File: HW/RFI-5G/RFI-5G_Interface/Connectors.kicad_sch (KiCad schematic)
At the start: 5 parts, among them J1 Conn_01x10_Female, J2 Conn_01x10_Female, J3 Conn_01x10_Female, J4 Conn_01x10_Female, J5 Conn_01x04_Female

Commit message: RF top and Bottom boards
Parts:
- removed J1, J2, J3, J4: Conn_01x10_Female, Connector_PinHeader_2.54mm:PinHeader_1x10_P2.54mm_Vertical, symbol Connector:Conn_01x10_Female
- removed J5: Conn_01x04_Female, Connector_PinHeader_2.54mm:PinHeader_1x04_P2.54mm_Vertical, symbol Connector:Conn_01x04_Female
- added J1, J4: Conn_01x03, Connector_PinHeader_2.54mm:PinHeader_1x03_P2.54mm_Vertical, symbol Connector_Generic:Conn_01x03
- added J2: Conn_01x02, Connector_PinHeader_2.54mm:PinHeader_1x02_P2.54mm_Vertical, symbol Connector_Generic:Conn_01x02
- added J3: Conn_01x10, Connector_PinHeader_2.54mm:PinHeader_1x10_P2.54mm_Vertical, symbol Connector_Generic:Conn_01x10
- added J5: Conn_01x06_Female, Connector_PinHeader_1.00mm:PinHeader_1x06_P1.00mm_Vertical, symbol Connector:Conn_01x06_Female
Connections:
- net ADC_PL2: now also J4.2 (Pin_2)
- net DAC_PL2: now also J4.3 (Pin_3)
- net GND: now also J1.3 (Pin_3), J2.1 (Pin_1), J3.10 (Pin_10), J3.3 (Pin_3), J3.4 (Pin_4), J4.1 (Pin_1)
- net SCL: now also J1.2 (Pin_2)
- net SDA: now also J1.1 (Pin_1)
- net VCC: now also J2.2 (Pin_2)
- new net 2V5: J5.2 (Pin_2)
- new net 2V7: J5.4 (Pin_4)
- new net 2V75: J3.1 (Pin_1), J5.6 (Pin_6)
- new net 3V: J3.8 (Pin_8)
- new net LDO_extra1: J5.3 (Pin_3)
- new net LDO_extra2: J5.5 (Pin_5)
- new net LEE1_Vcc: J3.6 (Pin_6)
- new net LEE2_Vcc: J3.7 (Pin_7)
- new net P/L power: J3.5 (Pin_5)
- new net RSSI: J3.9 (Pin_9)
- new net Vtune1: J5.1 (Pin_1)
- new net Vtune2: J3.2 (Pin_2)
- no-connect marks 11 -> 0
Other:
- note added: "Vcc will need to be changed to PoL whena pin for the point of load is available. Also, in the PCB, the Vcc zone will have to be changed to PoL."

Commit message: PL boards
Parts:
- removed J5: Conn_01x06_Female, Connector_PinHeader_1.00mm:PinHeader_1x06_P1.00mm_Vertical, symbol Connector:Conn_01x06_Female
- added J5: Conn_01x10_Female, Connector_PinHeader_1.00mm:PinHeader_1x10_P1.00mm_Vertical, symbol Connector:Conn_01x10_Female
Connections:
- net 3V: now also J5.8 (Pin_8)
- net GND: now also J5.7 (Pin_7)
- net SCL: now also J5.10 (Pin_10)
- net SDA: now also J5.9 (Pin_9)
- new net VTune1: J5.2 (Pin_2)
- new net Vcc_IF1Amp: J5.1 (Pin_1)
- new net Vcc_LNA1: J5.6 (Pin_6)
- new net Vcc_LNA2: J5.5 (Pin_5)
- new net Vcc_LO1Amp: J5.4 (Pin_4)
- new net Vcc_VCO: J5.3 (Pin_3)
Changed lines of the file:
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@@
+    (stroke (width 0) (type default) (color 0 0 0 0))
+  )
+  (wire (pts (xy 184.15 76.2) (xy 191.77 76.2))
     (stroke (width 0) (type default) (color 0 0 0 0))
   )
@@
     )
   )
-  (global_label "LDO_extra1" (shape input) (at 194.31 69.85 180) (fields_autoplaced)
-    (effects (font (size 1.27 1.27)) (justify right))
-    (property "Intersheet References" "${INTERSHEET_REFS}" (id 0) (at 181.3136 69.7706 0)
-      (effects (font (size 1.27 1.27)) (justify right) hide)
-    )
-  )
   (global_label "RSSI" (shape input) (at 151.13 93.98 90) (fields_autoplaced)
     (effects (font (size 1.27 1.27)) (justify left))
@@
     )
   )
-  (global_label "Vtune1" (shape input) (at 194.31 64.77 180) (fields_autoplaced)
-    (effects (font (size 1.27 1.27)) (justify right))
-    (property "Intersheet References" "${INTERSHEET_REFS}" (id 0) (at 185.4864 64.6906 0)
-      (effects (font (size 1.27 1.27)) (justify right) hide)
-    )
-  )
   (global_label "SCL" (shape bidirectional) (at 133.35 57.15 270) (fields_autoplaced)
     (effects (font (size 1.27 1.27)) (justify right))
@@
     )
   )
+  (global_label "SDA" (shape bidirectional) (at 191.77 81.28 180) (fields_autoplaced)
+    (effects (font (size 1.27 1.27)) (justify right))
+    (property "Intersheet References" "${INTERSHEET_REFS}" (id 0) (at 185.7888 81.2006 0)
+      (effects (font (size 1.27 1.27)) (justify right) hide)
+    )
+  )
   (global_label "LEE2_Vcc" (shape input) (at 146.05 93.98 90) (fields_autoplaced)
     (effects (font (size 1.27 1.27)) (justify left))
@@
     )
   )
-  (global_label "2V7" (shape input) (at 194.31 72.39 180) (fields_autoplaced)
-    (effects (font (size 1.27 1.27)) (justify right))
-    (property "Intersheet References" "${INTERSHEET_REFS}" (id 0) (at 188.3893 72.3106 0)
+  (global_label "Vcc_LNA1" (shape input) (at 191.77 73.66 180) (fields_autoplaced)
+    (effects (font (size 1.27 1.27)) (justify right))
+    (property "Intersheet References" "${INTERSHEET_REFS}" (id 0) (at 180.4669 73.5806 0)
       (effects (font (size 1.27 1.27)) (justify right) hide)
     )
@@
     )
   )
-  (global_label "2V75" (shape input) (at 194.31 77.47 180) (fields_autoplaced)
-    (effects (font (size 1.27 1.27)) (justify right))
-    (property "Intersheet References" "${INTERSHEET_REFS}" (id 0) (at 187.1798 77.3906 0)
+  (global_label "3V" (shape input) (at 191.77 78.74 180) (fields_autoplaced)
+    (effects (font (size 1.27 1.27)) (justify right))
+    (property "Intersheet References" "${INTERSHEET_REFS}" (id 0) (at 187.0588 78.6606 0)
       (effects (font (size 1.27 1.27)) (justify right) hide)
     )
@@
     )
   )
-  (global_label "2V5" (shape input) (at 194.31 67.31 180) (fields_autoplaced)
-    (effects (font (size 1.27 1.27)) (justify right))
-    (property "Intersheet References" "${INTERSHEET_REFS}" (id 0) (at 188.3893 67.2306 0)
+  (global_label "SCL" (shape bidirectional) (at 191.77 83.82 180) (fields_autoplaced)
+    (effects (font (size 1.27 1.27)) (justify right))
+    (property "Intersheet References" "${INTERSHEET_REFS}" (id 0) (at 185.8493 83.7406 0)
+      (effects (font (size 1.27 1.27)) (justify right) hide)
+    )
+  )
+  (global_label "Vcc_LNA2" (shape input) (at 191.77 71.12 180) (fields_autoplaced)
+    (effects (font (size 1.27 1.27)) (justify right))
+    (property "Intersheet References" "${INTERSHEET_REFS}" (id 0) (at 180.4669 71.0406 0)
       (effects (font (size 1.27 1.27)) (justify right) hide)
     )
@@
     )
   )
-  (global_label "LDO_extra2" (shape input) (at 194.31 74.93 180) (fields_autoplaced)
-    (effects (font (size 1.27 1.27)) (justify right))
-    (property "Intersheet References" "${INTERSHEET_REFS}" (id 0) (at 181.3136 74.8506 0)
+  (global_label "Vcc_IF1Amp" (shape input) (at 191.77 60.96 180) (fields_autoplaced)
+    (effects (font (size 1.27 1.27)) (justify right))
+    (property "Intersheet References" "${INTERSHEET_REFS}" (id 0) (at 178.2898 60.8806 0)
+      (effects (font (size 1.27 1.27)) (justify right) hide)
+    )
+  )
+  (global_label "Vcc_LO1Amp" (shape input) (at 191.77 68.58 180) (fields_autoplaced)
+    (effects (font (size 1.27 1.27)) (justify right))
+    (property "Intersheet References" "${INTERSHEET_REFS}" (id 0) (at 177.6245 68.5006 0)
+      (effects (font (size 1.27 1.27)) (justify right) hide)
+    )
+  )
+  (global_label "VTune1" (shape input) (at 191.77 63.5 180) (fields_autoplaced)
+    (effects (font (size 1.27 1.27)) (justify right))
+    (property "Intersheet References" "${INTERSHEET_REFS}" (id 0) (at 182.7045 63.4206 0)
+      (effects (font (size 1.27 1.27)) (justify right) hide)
+    )
+  )
+  (global_label "Vcc_VCO" (shape input) (at 191.77 66.04 180) (fields_autoplaced)
+    (effects (font (size 1.27 1.27)) (justify right))
+    (property "Intersheet References" "${INTERSHEET_REFS}" (id 0) (at 181.4345 65.9606 0)
       (effects (font (size 1.27 1.27)) (justify right) hide)
     )
@@
     (pin "3")
   )
-  (symbol (lib_id "Connector:Conn_01x06_Female") (at 199.39 69.85 0) (unit 1)
+  (symbol (lib_id "power:GND") (at 184.15 76.2 270) (unit 1)
+    (in_bom yes) (on_board yes)
+    (property "Reference" "#PWR?" (id 0) (at 177.8 76.2 0)
+      (effects (font (size 1.27 1.27)) hide)
+    )
+    (property "Value" "GND" (id 1) (at 179.07 74.93 0)
+      (effects (font (size 1.27 1.27)) (justify left))
+    )
+    (property "Footprint" "" (id 2) (at 184.15 76.2 0)
+      (effects (font (size 1.27 1.27)) hide)
+    )
+    (property "Datasheet" "" (id 3) (at 184.15 76.2 0)
+      (effects (font (size 1.27 1.27)) hide)
+    )
+    (pin "1")
+  )
+  (symbol (lib_id "power:VCC") (at 156.21 62.23 0) (unit 1)
     (in_bom yes) (on_board yes) (fields_autoplaced)
-    (property "Reference" "J5" (id 0) (at 200.66 71.1199 0)
+    (property "Reference" "#PWR0117" (id 0) (at 156.21 66.04 0)
+      (effects (font (size 1.27 1.27)) hide)
+    )
+    (property "Value" "VCC" (id 1) (at 158.75 60.9599 0)
       (effects (font (size 1.27 1.27)) (justify left))
     )
-    (property "Value" "Conn_01x06_Female" (id 1) (at 200.66 72.3899 0)
-      (effects (font (size 1.27 1.27)) (justify left) hide)
-    )
-    (property "Footprint" "Connector_PinHeader_1.00mm:PinHeader_1x06_P1.00mm_Vertical" (id 2) (at 199.39 69.85 0)
-      (effects (font (size 1.27 1.27)) hide)
-    )
-    (property "Datasheet" "~" (id 3) (at 199.39 69.85 0)
-      (effects (font (size 1.27 1.27)) hide)
-    )
-    (pin "1")
+    (property "Footprint" "" (id 2) (at 156.21 62.23 0)
+      (effects (font (size 1.27 1.27)) hide)
+    )
+    (property "Datasheet" "" (id 3) (at 156.21 62.23 0)
+      (effects (font (size 1.27 1.27)) hide)
+    )
+    (pin "1")
+  )
+  (symbol (lib_id "power:GND") (at 151.13 62.23 0) (unit 1)
+    (in_bom yes) (on_board yes) (fields_autoplaced)
+    (property "Reference" "#PWR0103" (id 0) (at 151.13 68.58 0)
+      (effects (font (size 1.27 1.27)) hide)
+    )
+    (property "Value" "GND" (id 1) (at 151.13 67.31 0))
+    (property "Footprint" "" (id 2) (at 151.13 62.23 0)
+      (effects (font (size 1.27 1.27)) hide)
+    )
+    (property "Datasheet" "" (id 3) (at 151.13 62.23 0)
+      (effects (font (size 1.27 1.27)) hide)
+    )
+    (pin "1")
+  )
+  (symbol (lib_id "Connector:Conn_01x10_Female") (at 196.85 71.12 0) (unit 1)
+    (in_bom yes) (on_board yes)
+    (property "Reference" "J5" (id 0) (at 193.04 57.15 0)
+      (effects (font (size 1.27 1.27)) (justify left))
+    )
+    (property "Value" "Conn_01x10_Female" (id 1) (at 198.12 73.6599 0)
+      (effects (font (size 1.27 1.27)) (justify left) hide)
+    )
+    (property "Footprint" "Connector_PinHeader_1.00mm:PinHeader_1x10_P1.00mm_Vertical" (id 2) (at 196.85 71.12 0)
+      (effects (font (size 1.27 1.27)) hide)
+    )
+    (property "Datasheet" "~" (id 3) (at 196.85 71.12 0)
+      (effects (font (size 1.27 1.27)) hide)
+    )
+    (pin "1")
+    (pin "10")
     (pin "2")
     (pin "3")
@@
     (pin "5")
     (pin "6")
-  )
-  (symbol (lib_id "power:VCC") (at 156.21 62.23 0) (unit 1)
-    (in_bom yes) (on_board yes) (fields_autoplaced)
-    (property "Reference" "#PWR0117" (id 0) (at 156.21 66.04 0)
-      (effects (font (size 1.27 1.27)) hide)
-    )
-    (property "Value" "VCC" (id 1) (at 158.75 60.9599 0)
-      (effects (font (size 1.27 1.27)) (justify left))
-    )
-    (property "Footprint" "" (id 2) (at 156.21 62.23 0)
-      (effects (font (size 1.27 1.27)) hide)
-    )
-    (property "Datasheet" "" (id 3) (at 156.21 62.23 0)
-      (effects (font (size 1.27 1.27)) hide)
-    )
-    (pin "1")
-  )
-  (symbol (lib_id "power:GND") (at 151.13 62.23 0) (unit 1)
-    (in_bom yes) (on_board yes) (fields_autoplaced)
-    (property "Reference" "#PWR0103" (id 0) (at 151.13 68.58 0)
-      (effects (font (size 1.27 1.27)) hide)
-    )
-    (property "Value" "GND" (id 1) (at 151.13 67.31 0))
-    (property "Footprint" "" (id 2) (at 151.13 62.23 0)
-      (effects (font (size 1.27 1.27)) hide)
-    )
-    (property "Datasheet" "" (id 3) (at 151.13 62.23 0)
-      (effects (font (size 1.27 1.27)) hide)
-    )
-    (pin "1")
+    (pin "7")
+    (pin "8")
+    (pin "9")
   )
   (symbol (lib_id "Connector_Generic:Conn_01x10") (at 140.97 99.06 90) (mirror x) (unit 1)

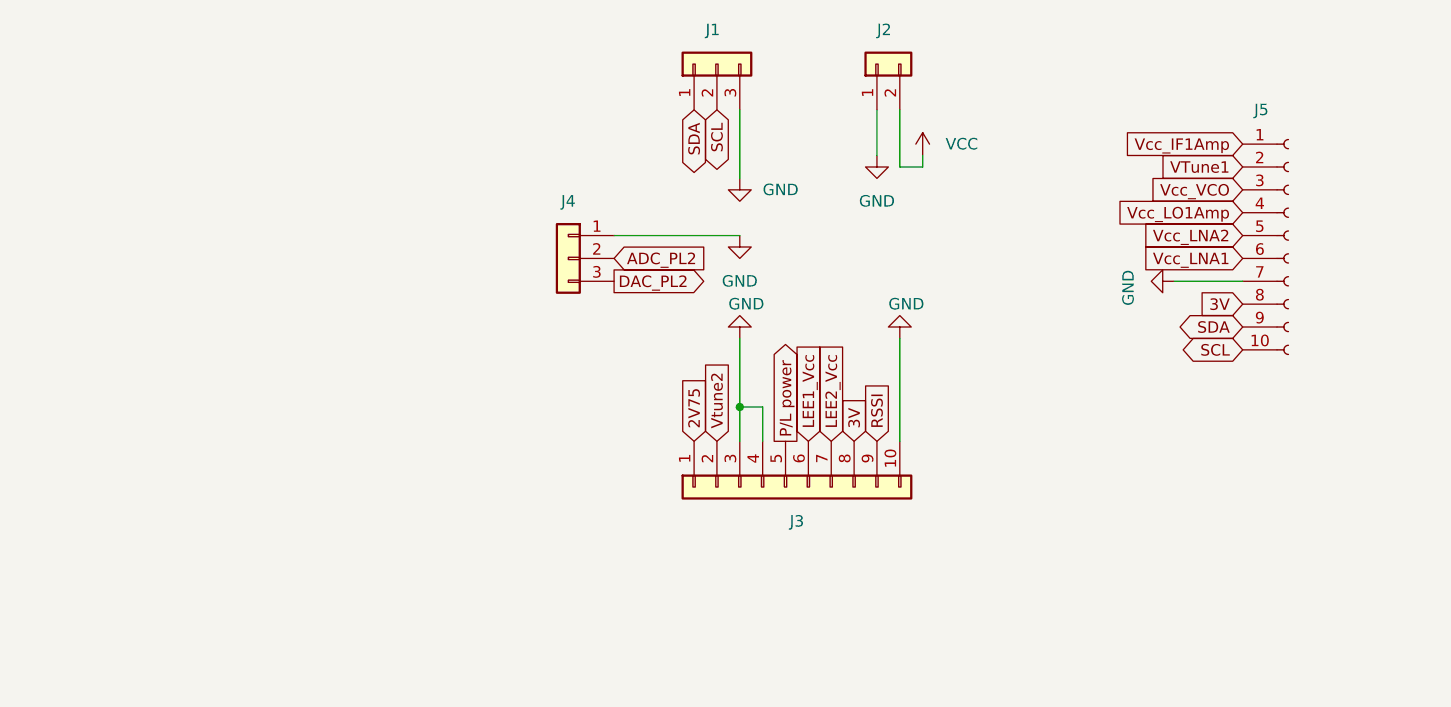
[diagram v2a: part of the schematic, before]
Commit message: All boards dseigned, thickness change pending
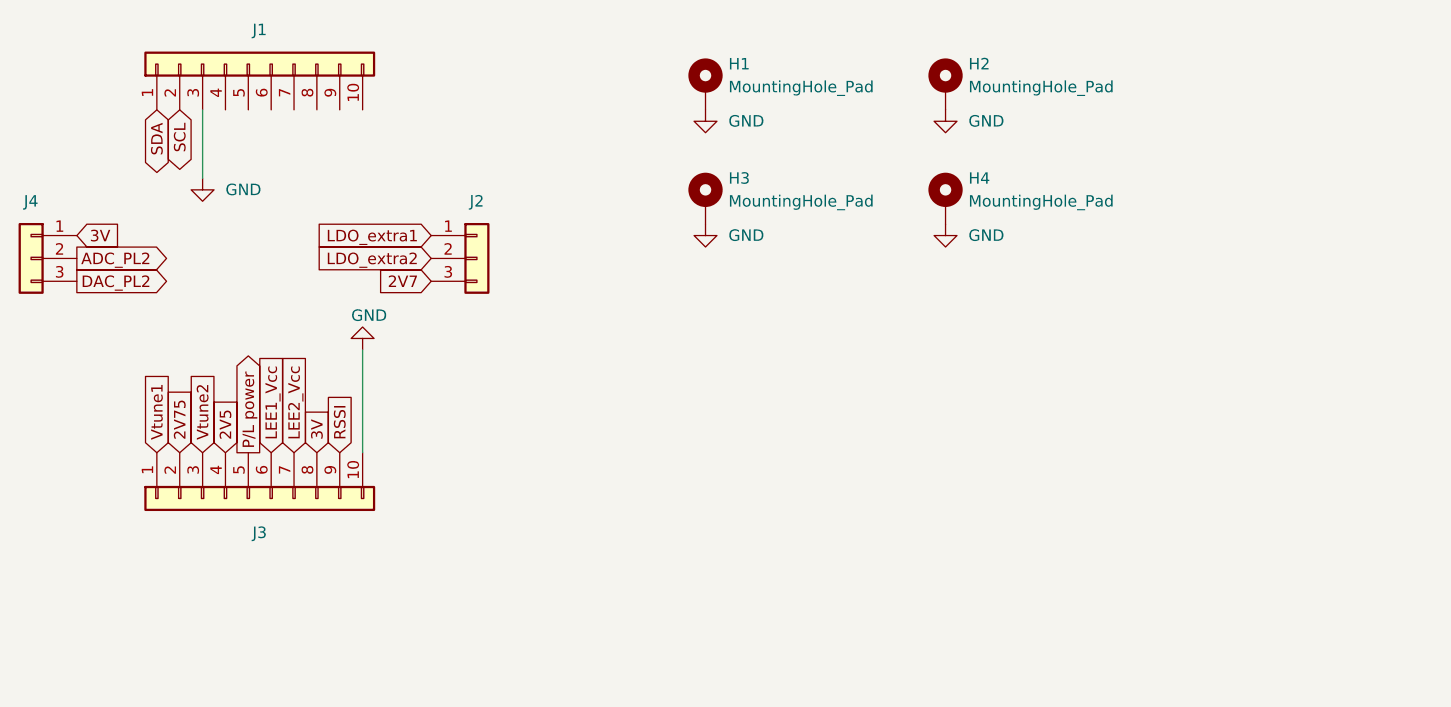
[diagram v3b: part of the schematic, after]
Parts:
- removed J1: Conn_01x03, Connector_PinHeader_2.54mm:PinHeader_1x03_P2.54mm_Vertical, symbol Connector_Generic:Conn_01x03
- removed J2: Conn_01x02, Connector_PinHeader_2.54mm:PinHeader_1x02_P2.54mm_Vertical, symbol Connector_Generic:Conn_01x02
- removed J5: Conn_01x10_Female, Connector_PinHeader_1.00mm:PinHeader_1x10_P1.00mm_Vertical, symbol Connector:Conn_01x10_Female
- added H1: MountingHole_Pad, symbol Mechanical:MountingHole_Pad
- added H2, H3, H4: MountingHole_Pad, MountingHole:MountingHole_3.5mm_Pad, symbol Mechanical:MountingHole_Pad
- added J1: Conn_01x10, Connector_PinHeader_2.54mm:PinHeader_1x10_P2.54mm_Vertical, symbol Connector_Generic:Conn_01x10
- added J2: Conn_01x03, Connector_PinHeader_2.54mm:PinHeader_1x03_P2.54mm_Vertical, symbol Connector_Generic:Conn_01x03
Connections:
- net 2V75: now also J3.2 (Pin_2); no longer J3.1 (Pin_1)
- net 3V: now also J4.1 (Pin_1)
- net GND: now also H1.1, H2.1, H3.1, H4.1, J1.3 (Pin_3); no longer J3.3 (Pin_3), J3.4 (Pin_4), J4.1 (Pin_1)
- net SCL: now also J1.2 (Pin_2)
- net SDA: now also J1.1 (Pin_1)
- net Vtune2: now also J3.3 (Pin_3); no longer J3.2 (Pin_2)
- new net 2V5: J3.4 (Pin_4)
- new net 2V7: J2.3 (Pin_3)
- new net LDO_extra1: J2.1 (Pin_1)
- new net LDO_extra2: J2.2 (Pin_2)
- new net Vtune1: J3.1 (Pin_1)
